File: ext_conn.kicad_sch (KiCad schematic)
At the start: 8 parts, among them J1 UDPI, J2 OUT, J3 USB_C, J4 CELL

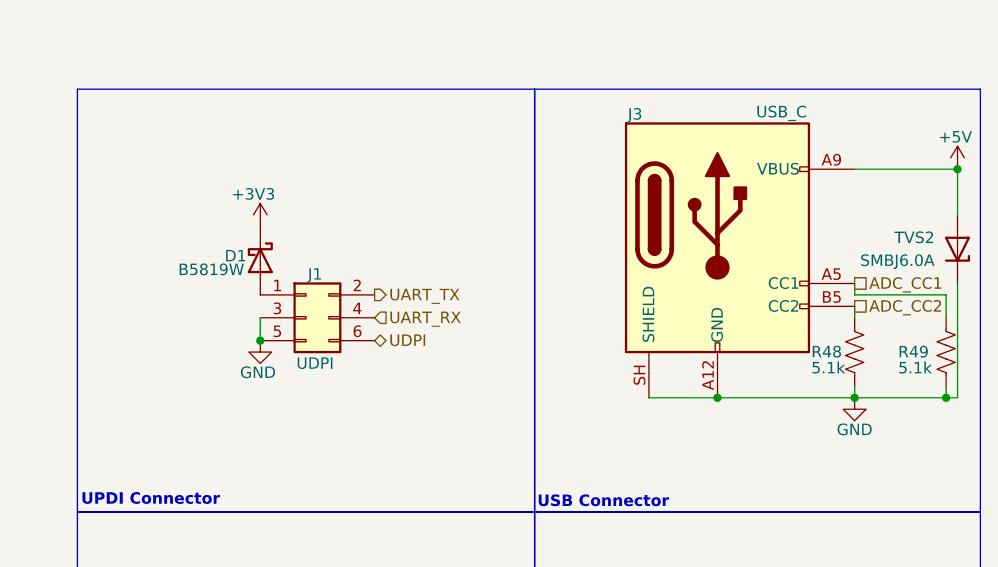
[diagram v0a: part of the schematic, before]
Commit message: Added labels and schematic PDF among other progress
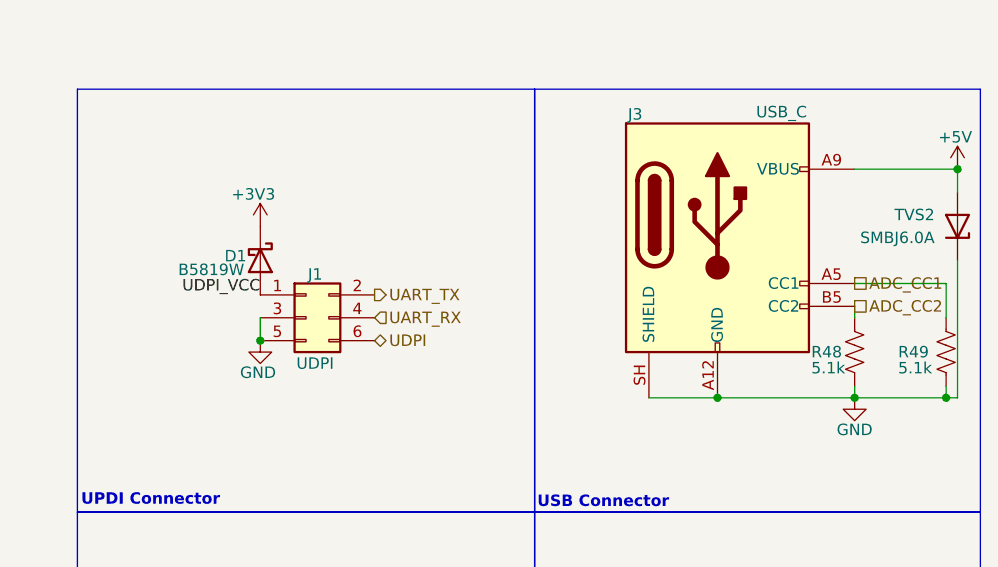
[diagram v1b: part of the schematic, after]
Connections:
- net UDPI_VCC: now reaches D1.2 (A), J1.1 (Pin_1)
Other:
- moved on the sheet: TVS2
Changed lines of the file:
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@@
 	(wire
 		(pts
-			(xy 184.15 69.85) (xy 184.15 72.39)
-		)
-		(stroke
-			(width 0)
-			(type default)
-		)
-	)
-	(wire
-		(pts
-			(xy 185.42 81.28) (xy 185.42 68.58)
+			(xy 184.15 68.58) (xy 184.15 72.39)
+		)
+		(stroke
+			(width 0)
+			(type default)
+		)
+	)
+	(wire
+		(pts
+			(xy 185.42 81.28) (xy 185.42 66.04)
 		)
 		(stroke
@@
 	(wire
 		(pts
-			(xy 173.99 69.85) (xy 184.15 69.85)
-		)
-		(stroke
-			(width 0)
-			(type default)
-		)
-	)
-	(wire
-		(pts
-			(xy 185.42 55.88) (xy 185.42 60.96)
+			(xy 173.99 68.58) (xy 184.15 68.58)
+		)
+		(stroke
+			(width 0)
+			(type default)
+		)
+	)
+	(wire
+		(pts
+			(xy 185.42 55.88) (xy 185.42 58.42)
 		)
 		(stroke
@@
 	(wire
 		(pts
-			(xy 173.99 69.85) (xy 173.99 68.58)
-		)
-		(stroke
-			(width 0)
-			(type default)
-		)
-	)
-	(wire
-		(pts
 			(xy 107.95 72.39) (xy 107.95 74.93)
 		)
@@
 			(width 0)
 			(type default)
+		)
+	)
+	(label "UDPI_VCC"
+		(at 107.95 69.85 180)
+		(effects
+			(font
+				(size 1.27 1.27)
+			)
+			(justify right bottom)
 		)
 	)
@@
 	(symbol
 		(lib_id "Device:D_Zener")
-		(at 185.42 64.77 270)
+		(at 185.42 62.23 270)
 		(mirror x)
 		(unit 1)
@@
 		(dnp no)
 		(property "Reference" "TVS2"
+			(at 182.88 60.9599 90)
+			(show_name no)
+			(do_not_autoplace no)
+			(effects
+				(font
+					(size 1.27 1.27)
+				)
+				(justify right)
+			)
+		)
+		(property "Value" "SMBJ6.0A"
 			(at 182.88 63.4999 90)
 			(show_name no)
@@
 			)
 		)
-		(property "Value" "SMBJ6.0A"
-			(at 182.88 66.0399 90)
-			(show_name no)
-			(do_not_autoplace no)
-			(effects
-				(font
-					(size 1.27 1.27)
-				)
-				(justify right)
-			)
-		)
 		(property "Footprint" "Diode_SMD:D_SMB"
-			(at 185.42 64.77 0)
+			(at 185.42 62.23 0)
 			(hide yes)
 			(show_name no)
@@
 		)
 		(property "Datasheet" ""
-			(at 185.42 64.77 0)
+			(at 185.42 62.23 0)
 			(hide yes)
 			(show_name no)
@@
 		)
 		(property "Description" "TVS diode"
-			(at 185.42 64.77 0)
+			(at 185.42 62.23 0)
 			(hide yes)
 			(show_name no)
@@
 		)
 		(property "LCSC#" "C140903"
-			(at 185.42 64.77 90)
+			(at 185.42 62.23 90)
 			(hide yes)
 			(show_name no)
@@
 		)
 		(property "MFR#" "SMBJ6.0A"
-			(at 185.42 64.77 90)
-			(hide yes)
-			(show_name no)
+			(at 185.42 62.23 90)
+			(hide yes)
+			(show_name no)

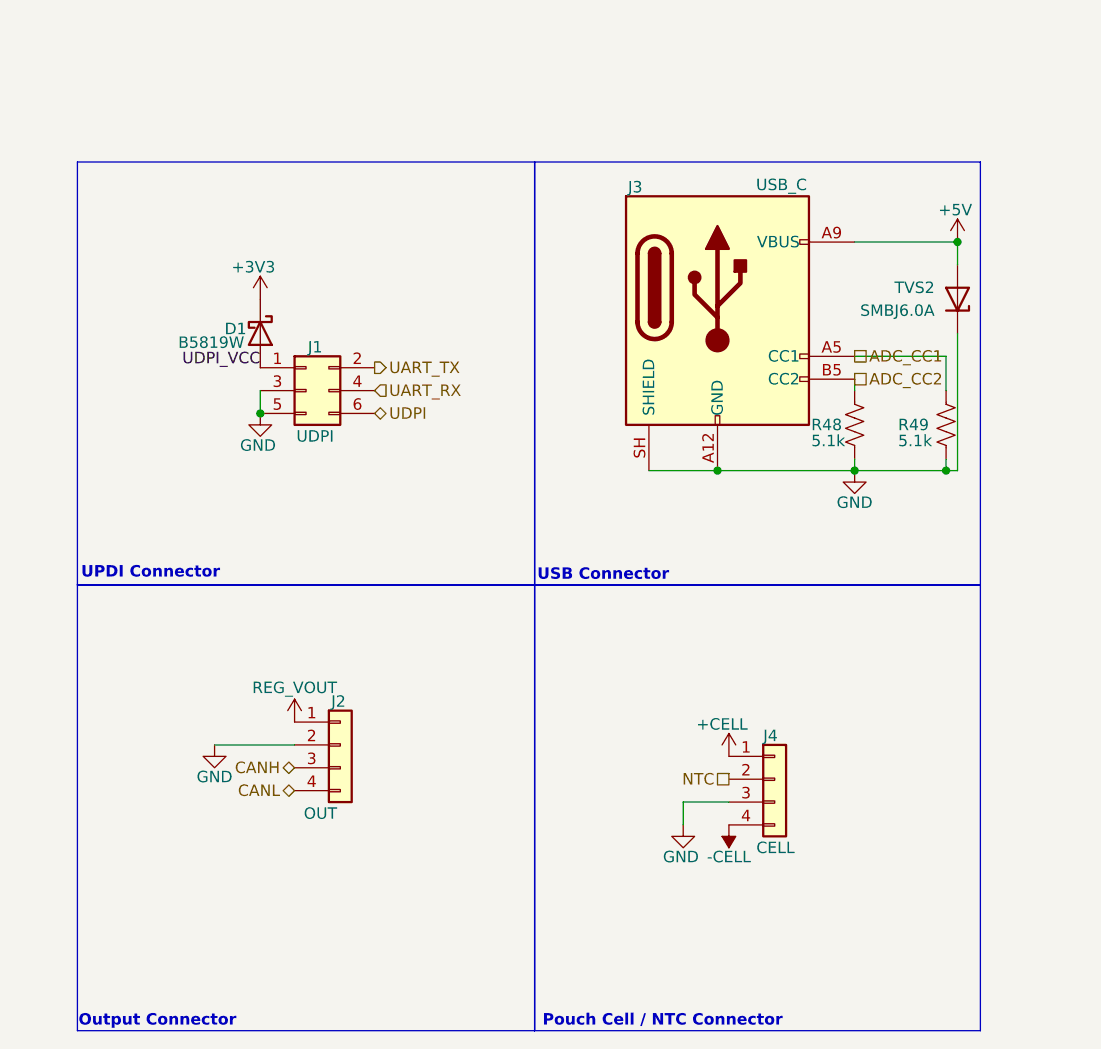
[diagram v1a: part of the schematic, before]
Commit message: Added testpoints
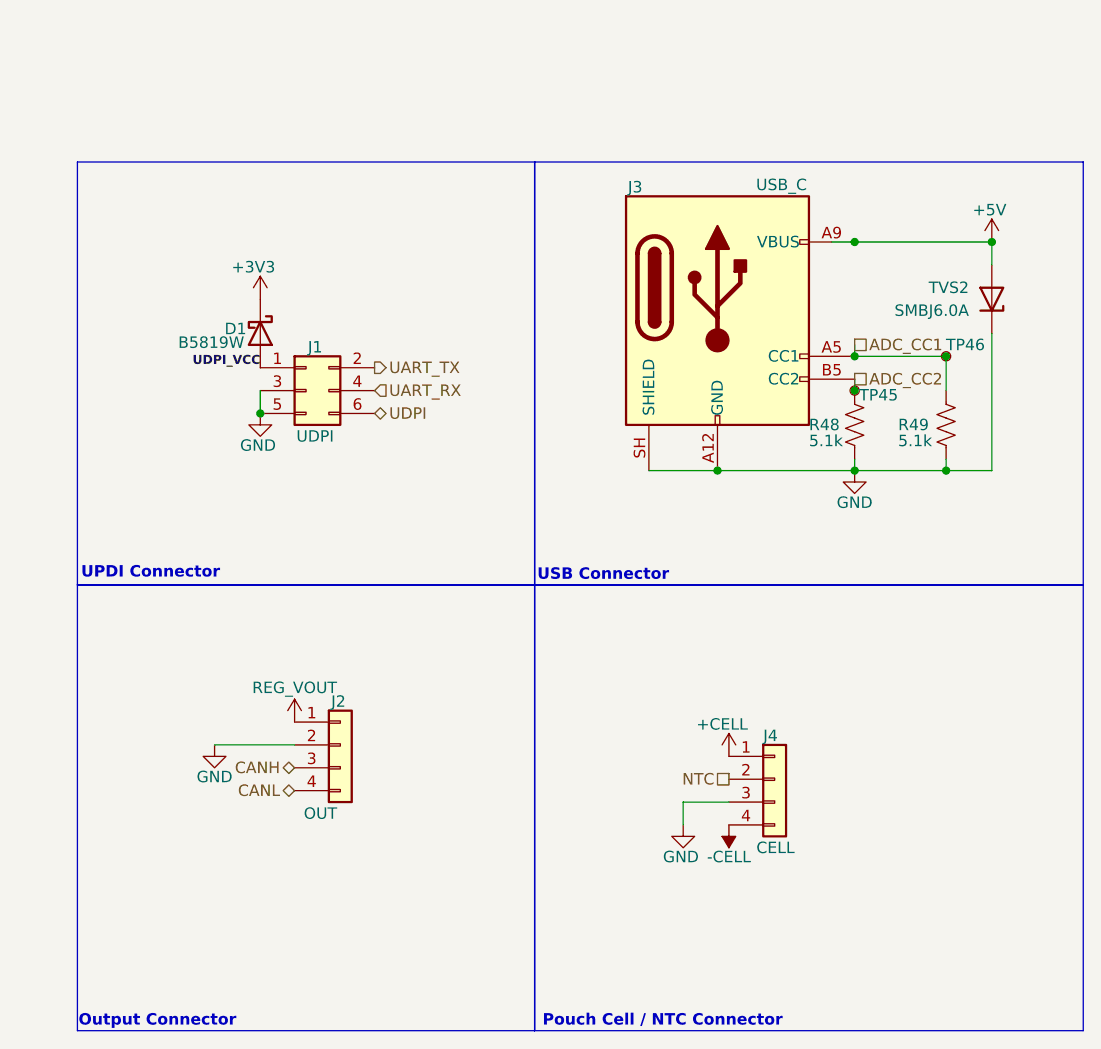
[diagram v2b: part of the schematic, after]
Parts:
- added TP45: ADC_CC2, symbol Connector:TestPoint_Small
- added TP46: ADC_CC1, symbol Connector:TestPoint_Small
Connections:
- net ADC_CC1: now also TP46.1
- net ADC_CC2: now also TP45.1
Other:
- moved on the sheet: TVS2

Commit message: Partially assigned netclasses WIP
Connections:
- net UDPI renamed UPDI
- net UDPI_VCC renamed UPDI_VCC
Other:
- moved on the sheet: D1, R48, R49

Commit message: Configured Varients
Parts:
- renumbered R48 to R49, R49 to R50
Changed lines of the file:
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@@
 		(in_pos_files yes)
 		(dnp no)
-		(property "Reference" "#PWR059"
+		(property "Reference" "#PWR058"
 			(at 154.94 115.57 0)
 			(hide yes)
@@
 			(project "power_module"
 				(path "/33e2b92e-f705-4be7-96f4-57092b8ec1ea/a7e85cd0-99ff-418b-b157-324cad7ee261"
-					(reference "#PWR059")
+					(reference "#PWR058")
 					(unit 1)
 				)
@@
 		(in_pos_files yes)
 		(dnp no)
-		(property "Reference" "R48"
+		(property "Reference" "R49"
 			(at 168.91 78.74 0)
 			(show_name no)
@@
 			(project "power_module"
 				(path "/33e2b92e-f705-4be7-96f4-57092b8ec1ea/a7e85cd0-99ff-418b-b157-324cad7ee261"
-					(reference "R48")
+					(reference "R49")
 					(unit 1)
 				)
@@
 		(in_pos_files yes)
 		(dnp no)
-		(property "Reference" "R49"
+		(property "Reference" "R50"
 			(at 178.816 78.74 0)
 			(show_name no)
@@
 			(project "power_module"
 				(path "/33e2b92e-f705-4be7-96f4-57092b8ec1ea/a7e85cd0-99ff-418b-b157-324cad7ee261"
-					(reference "R49")
+					(reference "R50")
 					(unit 1)
 				)
@@
 		(in_pos_files yes)
 		(dnp no)
-		(property "Reference" "#PWR058"
+		(property "Reference" "#PWR059"
 			(at 154.94 128.27 0)
 			(hide yes)
@@
 			(project "power_module"
 				(path "/33e2b92e-f705-4be7-96f4-57092b8ec1ea/a7e85cd0-99ff-418b-b157-324cad7ee261"
-					(reference "#PWR058")
-					(unit 1)
-				)
+					(reference "#PWR059")
+					(unit 1)
+				)

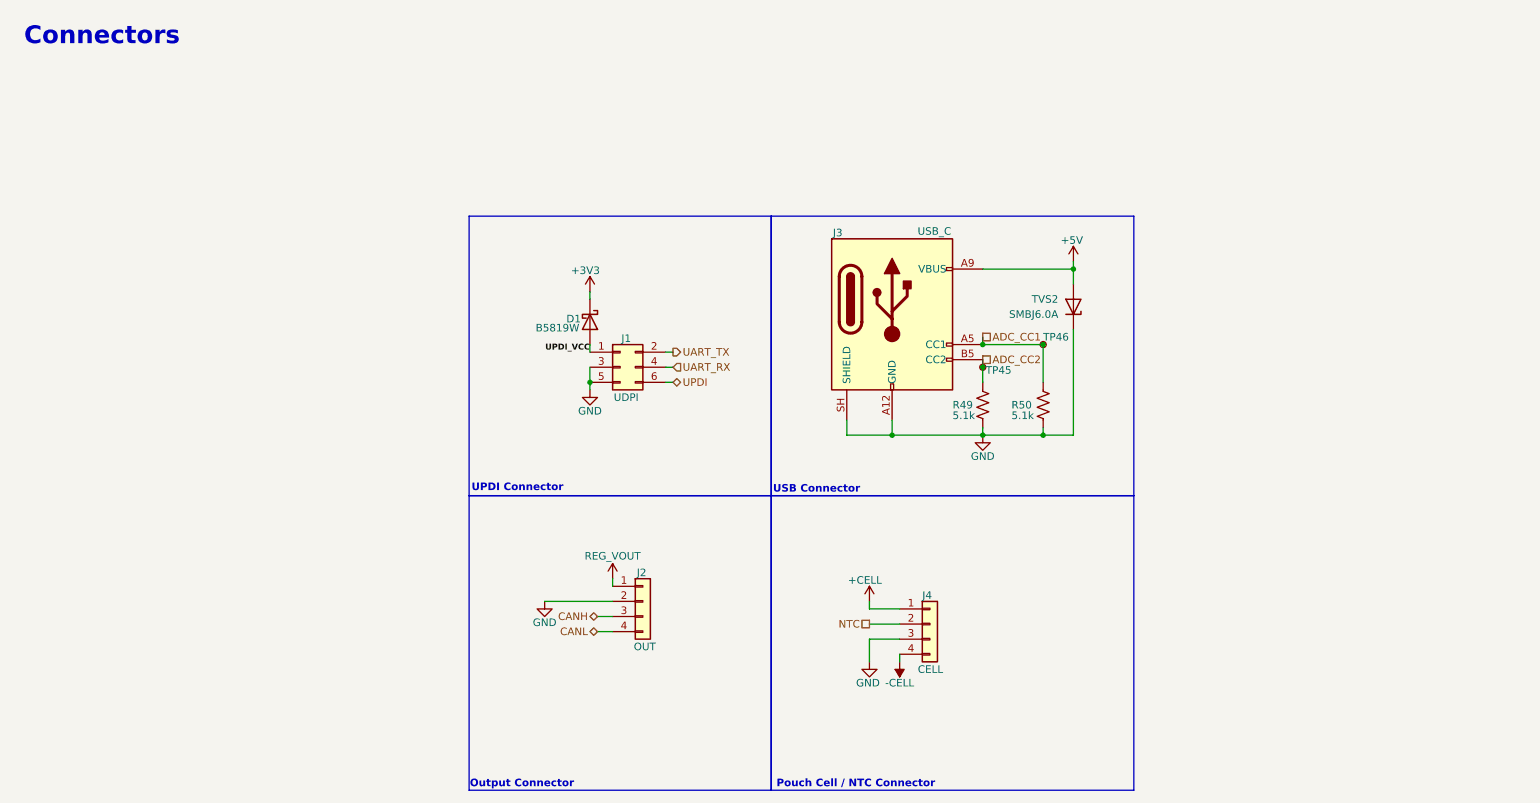
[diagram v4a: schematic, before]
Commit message: Started work on PCB layout
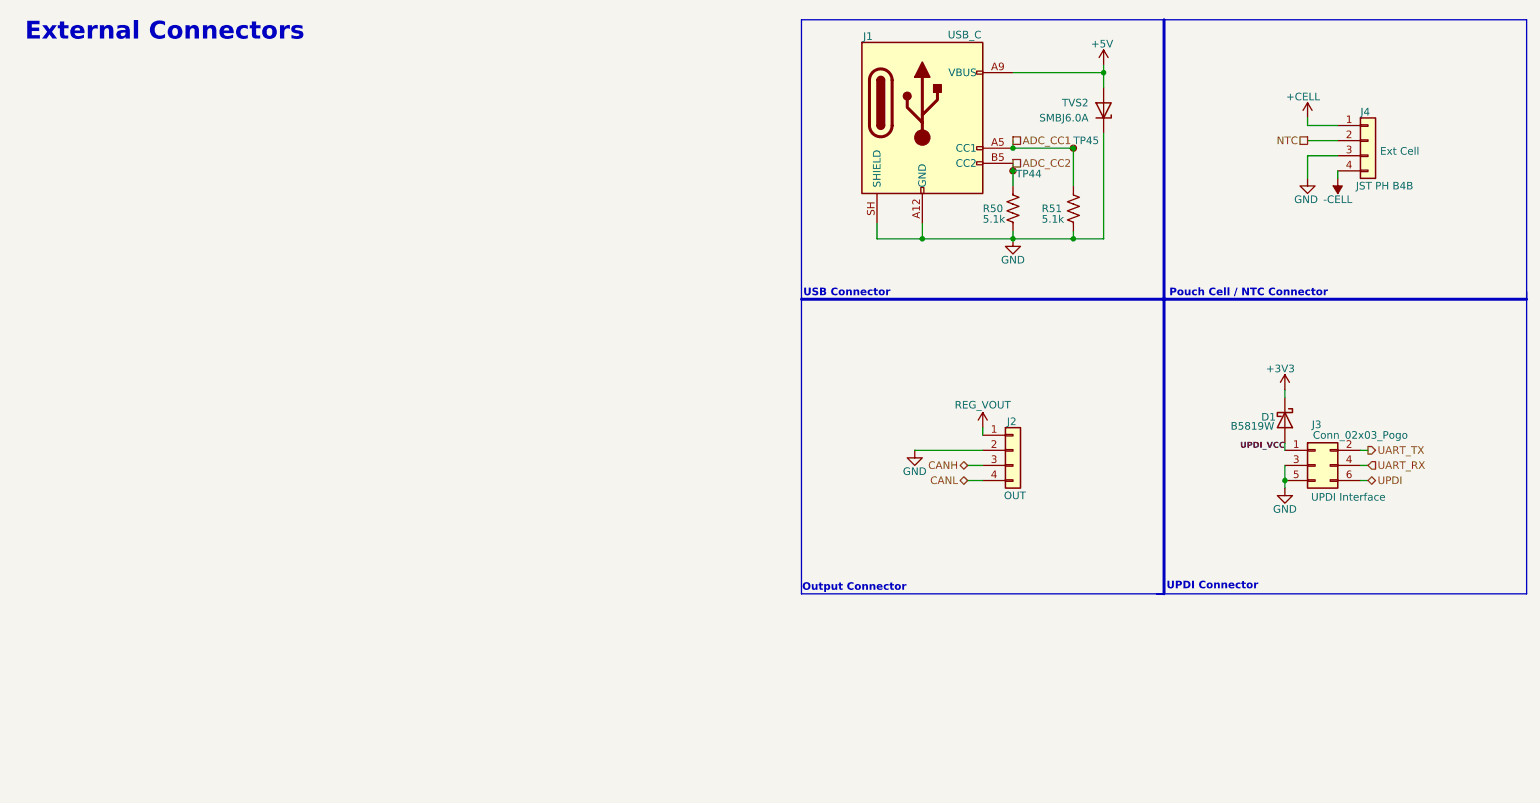
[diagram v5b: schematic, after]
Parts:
- J3: renamed from J1; value UDPI -> Conn_02x03_Pogo
- J4: value CELL -> JST PH B4B
- TP44: renamed from TP45; footprint (none) -> TestPoint:TestPoint_Pad_D1.0mm
- TP45: renamed from TP46; footprint (none) -> TestPoint:TestPoint_Pad_D1.0mm
- renumbered J3 to J1, R49 to R50, R50 to R51
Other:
- note added: "External Connectors"
- note removed: "Connectors"
- moved on the sheet: D1, J1, J2, J3, J4, R50, R51, TP44, TP45, TVS2

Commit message: Initial commit
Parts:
- J2: value OUT -> JST_PH
- J4: value JST PH B4B -> JST_PH
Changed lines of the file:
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@@
 			)
 		)
-		(property "Value" "JST PH B4B"
+		(property "Value" "JST_PH"
 			(at 236.728 41.91 0)
 			(show_name no)
@@
 		)
 		(property "Description" "Ext Cell"
-			(at 244.094 36.068 0)
+			(at 240.792 43.688 0)
 			(show_name no)
 			(do_not_autoplace no)
@@
 			)
 		)
-		(property "Value" "OUT"
+		(property "Value" "JST_PH"
 			(at 177.546 93.98 0)
 			(show_name no)
@@
 			)
 		)
-		(property "Description" "Generic connector, single row, 01x04, script generated (kicad-library-utils/schlib/autogen/connector/)"
-			(at 179.07 86.36 0)
-			(hide yes)
-			(show_name no)
-			(do_not_autoplace no)
+		(property "Description" "External"
+			(at 181.61 96.012 0)
+			(show_name no)
+			(do_not_autoplace no)
